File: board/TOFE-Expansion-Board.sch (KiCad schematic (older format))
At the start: 6 parts, among them U1 TOFE-8X, U7 24AA01/24LC01B

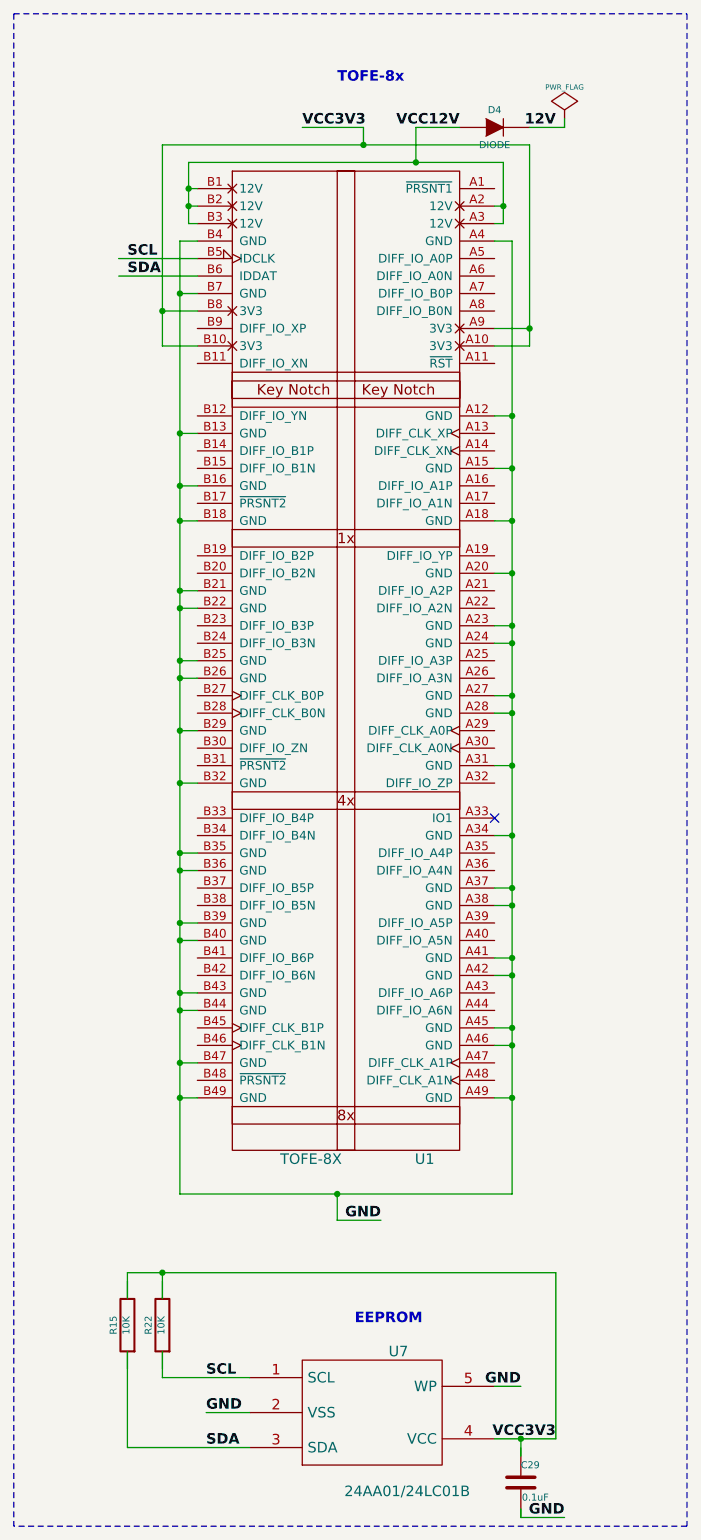
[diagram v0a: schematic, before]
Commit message: Improving the EEPROM schematic.
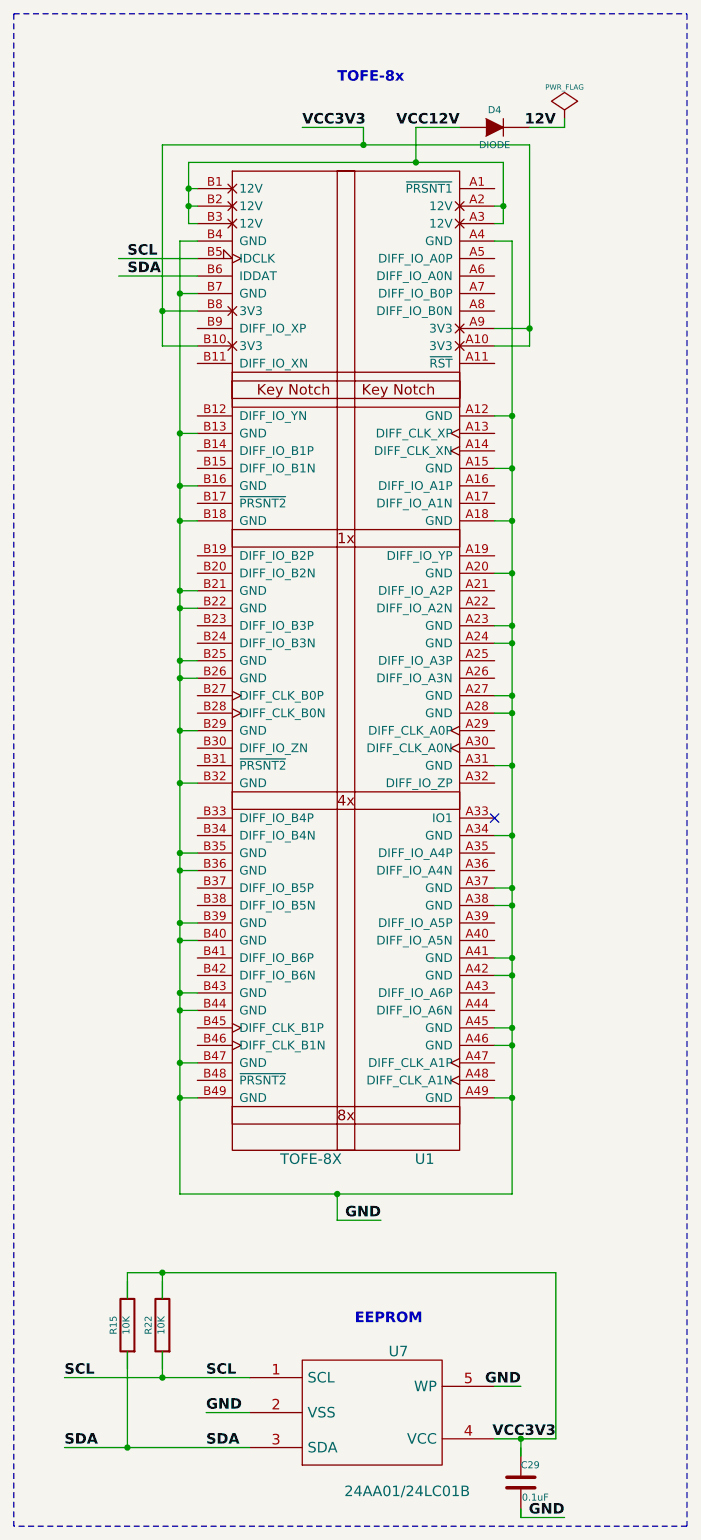
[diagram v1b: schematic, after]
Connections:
- wire segments 124 -> 79
